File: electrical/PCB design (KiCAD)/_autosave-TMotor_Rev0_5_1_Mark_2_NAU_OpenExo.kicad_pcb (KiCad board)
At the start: 2 copper layers, 89.4 x 82.6 mm, 96 parts, among them J1 Conn_01x07_Pin, J10 XT30PW-F, J11 XT30PW-F, J12 XT30PW-F, J13 TFM-107-01-L-D-WT, J2 Conn_01x04_Pin, J3 Conn_01x02_Pin, J4 Conn_01x02_Pin, J5 Conn_01x02_Pin, J6 Conn_01x02_Pin, J7 Conn_01x03_Pin, J8 XT30PW-F, J9 XT30PW-F, U1 TXU0104PWR, U10 DEV-16771, U2 TXU0304-Q1, U3 INA125U, U4 INA125U, U5 SN65HVD230DR, U6 INA125U, U7 INA125U

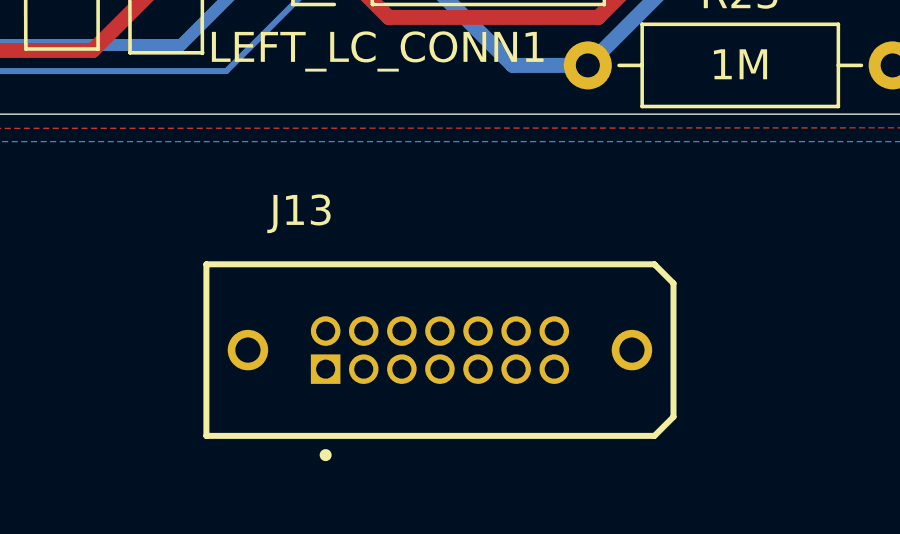
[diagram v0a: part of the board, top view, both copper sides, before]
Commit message: Initial version for bluetooth (BLE) handler with central and peripheral implementation
Central uses Python library BLEAK and connects to the peripheral (Arduino Nano)
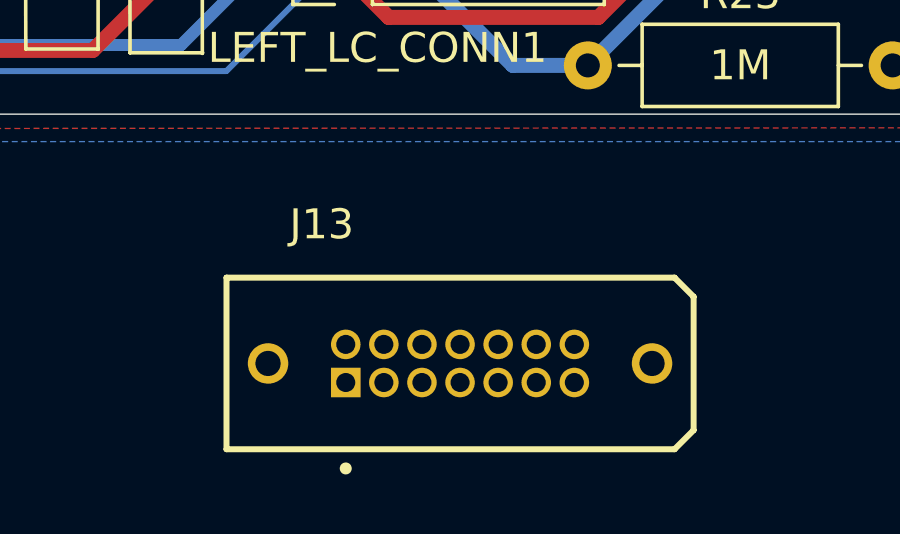
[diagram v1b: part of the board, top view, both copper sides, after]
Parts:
- moved J13 0.80 mm to (149.6, 154.9)
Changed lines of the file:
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@@
 	(footprint "ISDF connector:SAMTEC_TFM-107-01-L-D-WT"
 		(layer "F.Cu")
-		(at 148.9 154.49)
+		(at 149.57 154.935)
 		(property "Reference" "J13"
 			(at -4.61 -4.635 0)
